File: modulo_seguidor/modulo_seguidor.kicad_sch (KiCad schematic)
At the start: 12 parts, among them J1 Battery, J4 Motor Izquierdo, J5 Motor Derecho, J6 puerto sensores, SW1 SW_Push, U1 LM7806_TO220

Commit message: feat: Asigno las huellas a los componentes
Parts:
- C1: value C -> 1u; footprint (none) -> Capacitor_THT:C_Disc_D7.5mm_W5.0mm_P10.00mm
- C2: footprint (none) -> Capacitor_THT:C_Disc_D7.5mm_W5.0mm_P10.00mm
- D1: footprint (none) -> LED_THT:LED_D3.0mm
- J1: footprint (none) -> Connector_Molex:Molex_KK-254_AE-6410-02A_1x02_P2.54mm_Vertical
- J4, J5: footprint (none) -> Connector:FanPinHeader_1x03_P2.54mm_Vertical
- J6: footprint (none) -> Connector_Harwin:Harwin_M20-89008xx_1x08_P2.54mm_Horizontal
- R1, R2: footprint (none) -> Resistor_THT:R_Axial_DIN0204_L3.6mm_D1.6mm_P5.08mm_Horizontal
- SW1: footprint (none) -> Button_Switch_THT:SW_PUSH_6mm
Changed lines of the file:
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@@
 			)
 		)
-		(property "Footprint" ""
+		(property "Footprint" "Capacitor_THT:C_Disc_D7.5mm_W5.0mm_P10.00mm"
 			(at 77.1652 111.76 0)
 			(effects
@@
 			)
 		)
-		(property "Footprint" ""
+		(property "Footprint" "Button_Switch_THT:SW_PUSH_6mm"
 			(at 113.03 113.03 0)
 			(effects
@@
 			)
 		)
-		(property "Footprint" ""
+		(property "Footprint" "LED_THT:LED_D3.0mm"
 			(at 133.35 62.23 0)
 			(effects
@@
 			)
 		)
-		(property "Footprint" ""
+		(property "Footprint" "Connector:FanPinHeader_1x03_P2.54mm_Vertical"
 			(at 196.85 130.81 0)
 			(effects
@@
 			)
 		)
-		(property "Footprint" ""
+		(property "Footprint" "Connector:FanPinHeader_1x03_P2.54mm_Vertical"
 			(at 171.45 130.81 0)
 			(effects
@@
 			)
 		)
-		(property "Footprint" ""
+		(property "Footprint" "Connector_Harwin:Harwin_M20-89008xx_1x08_P2.54mm_Horizontal"
 			(at 237.49 91.44 0)
 			(effects
@@
 			)
 		)
-		(property "Footprint" ""
+		(property "Footprint" "Resistor_THT:R_Axial_DIN0204_L3.6mm_D1.6mm_P5.08mm_Horizontal"
 			(at 125.984 67.564 90)
 			(effects
@@
 			)
 		)
-		(property "Footprint" ""
+		(property "Footprint" "Connector_Molex:Molex_KK-254_AE-6410-02A_1x02_P2.54mm_Vertical"
 			(at 53.34 69.85 0)
 			(effects
@@
 			)
 		)
-		(property "Footprint" ""
+		(property "Footprint" "Resistor_THT:R_Axial_DIN0204_L3.6mm_D1.6mm_P5.08mm_Horizontal"
 			(at 107.696 123.444 90)
 			(effects
@@
 			)
 		)
-		(property "Value" "C"
+		(property "Value" "1u"
 			(at 76.2 69.8499 0)
 			(effects
@@
 			)
 		)
-		(property "Footprint" ""
+		(property "Footprint" "Capacitor_THT:C_Disc_D7.5mm_W5.0mm_P10.00mm"
 			(at 73.3552 72.39 0)
 			(effects

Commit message: refactor: Actualizo huellas del esquemático
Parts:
- C1, C2: footprint Capacitor_THT:C_Disc_D7.5mm_W5.0mm_P10.00mm -> Capacitor_THT:C_Disc_D7.0mm_W2.5mm_P5.00mm
- D1: footprint LED_THT:LED_D3.0mm -> LED_THT:LED_D5.0mm
- J4, J5: footprint Connector:FanPinHeader_1x03_P2.54mm_Vertical -> Connector_PinHeader_2.54mm:PinHeader_1x03_P2.54mm_Vertical
- J6: footprint Connector_Harwin:Harwin_M20-89008xx_1x08_P2.54mm_Horizontal -> Connector_PinHeader_2.54mm:PinHeader_1x08_P2.54mm_Horizontal
- R1, R2: footprint Resistor_THT:R_Axial_DIN0204_L3.6mm_D1.6mm_P5.08mm_Horizontal -> Resistor_THT:R_Axial_DIN0411_L9.9mm_D3.6mm_P12.70mm_Horizontal
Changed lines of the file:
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@@
 			)
 		)
-		(property "Footprint" "Capacitor_THT:C_Disc_D7.5mm_W5.0mm_P10.00mm"
+		(property "Footprint" "Capacitor_THT:C_Disc_D7.0mm_W2.5mm_P5.00mm"
 			(at 77.1652 111.76 0)
 			(effects
@@
 			)
 		)
-		(property "Footprint" "LED_THT:LED_D3.0mm"
+		(property "Footprint" "LED_THT:LED_D5.0mm"
 			(at 133.35 62.23 0)
 			(effects
@@
 			)
 		)
-		(property "Footprint" "Connector:FanPinHeader_1x03_P2.54mm_Vertical"
+		(property "Footprint" "Connector_PinHeader_2.54mm:PinHeader_1x03_P2.54mm_Vertical"
 			(at 196.85 130.81 0)
 			(effects
@@
 			)
 		)
-		(property "Footprint" "Connector:FanPinHeader_1x03_P2.54mm_Vertical"
+		(property "Footprint" "Connector_PinHeader_2.54mm:PinHeader_1x03_P2.54mm_Vertical"
 			(at 171.45 130.81 0)
 			(effects
@@
 			)
 		)
-		(property "Footprint" "Connector_Harwin:Harwin_M20-89008xx_1x08_P2.54mm_Horizontal"
+		(property "Footprint" "Connector_PinHeader_2.54mm:PinHeader_1x08_P2.54mm_Horizontal"
 			(at 237.49 91.44 0)
 			(effects
@@
 			)
 		)
-		(property "Footprint" "Resistor_THT:R_Axial_DIN0204_L3.6mm_D1.6mm_P5.08mm_Horizontal"
+		(property "Footprint" "Resistor_THT:R_Axial_DIN0411_L9.9mm_D3.6mm_P12.70mm_Horizontal"
 			(at 125.984 67.564 90)
 			(effects
@@
 			)
 		)
-		(property "Footprint" "Resistor_THT:R_Axial_DIN0204_L3.6mm_D1.6mm_P5.08mm_Horizontal"
+		(property "Footprint" "Resistor_THT:R_Axial_DIN0411_L9.9mm_D3.6mm_P12.70mm_Horizontal"
 			(at 107.696 123.444 90)
 			(effects
@@
 			)
 		)
-		(property "Footprint" "Capacitor_THT:C_Disc_D7.5mm_W5.0mm_P10.00mm"
+		(property "Footprint" "Capacitor_THT:C_Disc_D7.0mm_W2.5mm_P5.00mm"
 			(at 73.3552 72.39 0)
 			(effects

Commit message: refactor: Cambio las conexiones en los pines del modulo seguidor para compactar la pcb
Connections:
- net Boton_encendido: now also A2.D10; no longer A2.D2 (D2_INT0)
- net PWM_DER: now also A2.D8; no longer A2.D9
- net PWM_IZQ: now also A2.D9; no longer A2.D10
- net Sensor1: now also A2.D7; no longer A2.D8
- net Sensor2: now also A2.D6; no longer A2.D7
- net Sensor3: now also A2.D5; no longer A2.D6
- net Sensor4: now also A2.D4; no longer A2.D5
- net Sensor5: now also A2.D3 (D3_INT1); no longer A2.D4
- net Sensor6: now also A2.D2 (D2_INT0); no longer A2.D3 (D3_INT1)
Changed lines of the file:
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@@
 	)
 	(label "Sensor1"
-		(at 190.5 67.31 0)
+		(at 190.5 64.77 0)
 		(fields_autoplaced yes)
 		(effects
@@
 	)
 	(label "PWM_IZQ"
-		(at 190.5 72.39 0)
+		(at 190.5 69.85 0)
 		(fields_autoplaced yes)
 		(effects
@@
 	)
 	(label "Sensor3"
-		(at 190.5 62.23 0)
+		(at 190.5 59.69 0)
 		(fields_autoplaced yes)
 		(effects
@@
 	)
 	(label "Boton_encendido"
-		(at 190.5 52.07 0)
+		(at 190.5 72.39 0)
 		(fields_autoplaced yes)
 		(effects
@@
 	)
 	(label "Sensor2"
-		(at 190.5 64.77 0)
+		(at 190.5 62.23 0)
 		(fields_autoplaced yes)
 		(effects
@@
 	)
 	(label "Sensor4"
-		(at 190.5 59.69 0)
+		(at 190.5 57.15 0)
 		(fields_autoplaced yes)
 		(effects
@@
 	)
 	(label "PWM_DER"
-		(at 190.5 69.85 0)
+		(at 190.5 67.31 0)
 		(fields_autoplaced yes)
 		(effects
@@
 	)
 	(label "Sensor5"
-		(at 190.5 57.15 0)
+		(at 190.5 54.61 0)
 		(fields_autoplaced yes)
 		(effects
@@
 	)
 	(label "Sensor6"
-		(at 190.5 54.61 0)
+		(at 190.5 52.07 0)
 		(fields_autoplaced yes)
 		(effects

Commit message: refactor(modulo_seguidor): Intercambio dos pines para hacer los cables más cortos
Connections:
- net Boton_encendido: now also A2.D8; no longer A2.D10
- net PWM_DER: now also A2.D9; no longer A2.D8
- net PWM_IZQ: now also A2.D10; no longer A2.D9
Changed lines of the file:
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@@
 	)
 	(label "PWM_IZQ"
-		(at 190.5 69.85 0)
+		(at 190.5 72.39 0)
 		(fields_autoplaced yes)
 		(effects
@@
 	)
 	(label "Boton_encendido"
-		(at 190.5 72.39 0)
+		(at 190.5 67.31 0)
 		(fields_autoplaced yes)
 		(effects
@@
 	)
 	(label "PWM_DER"
-		(at 190.5 67.31 0)
+		(at 190.5 69.85 0)
 		(fields_autoplaced yes)
 		(effects

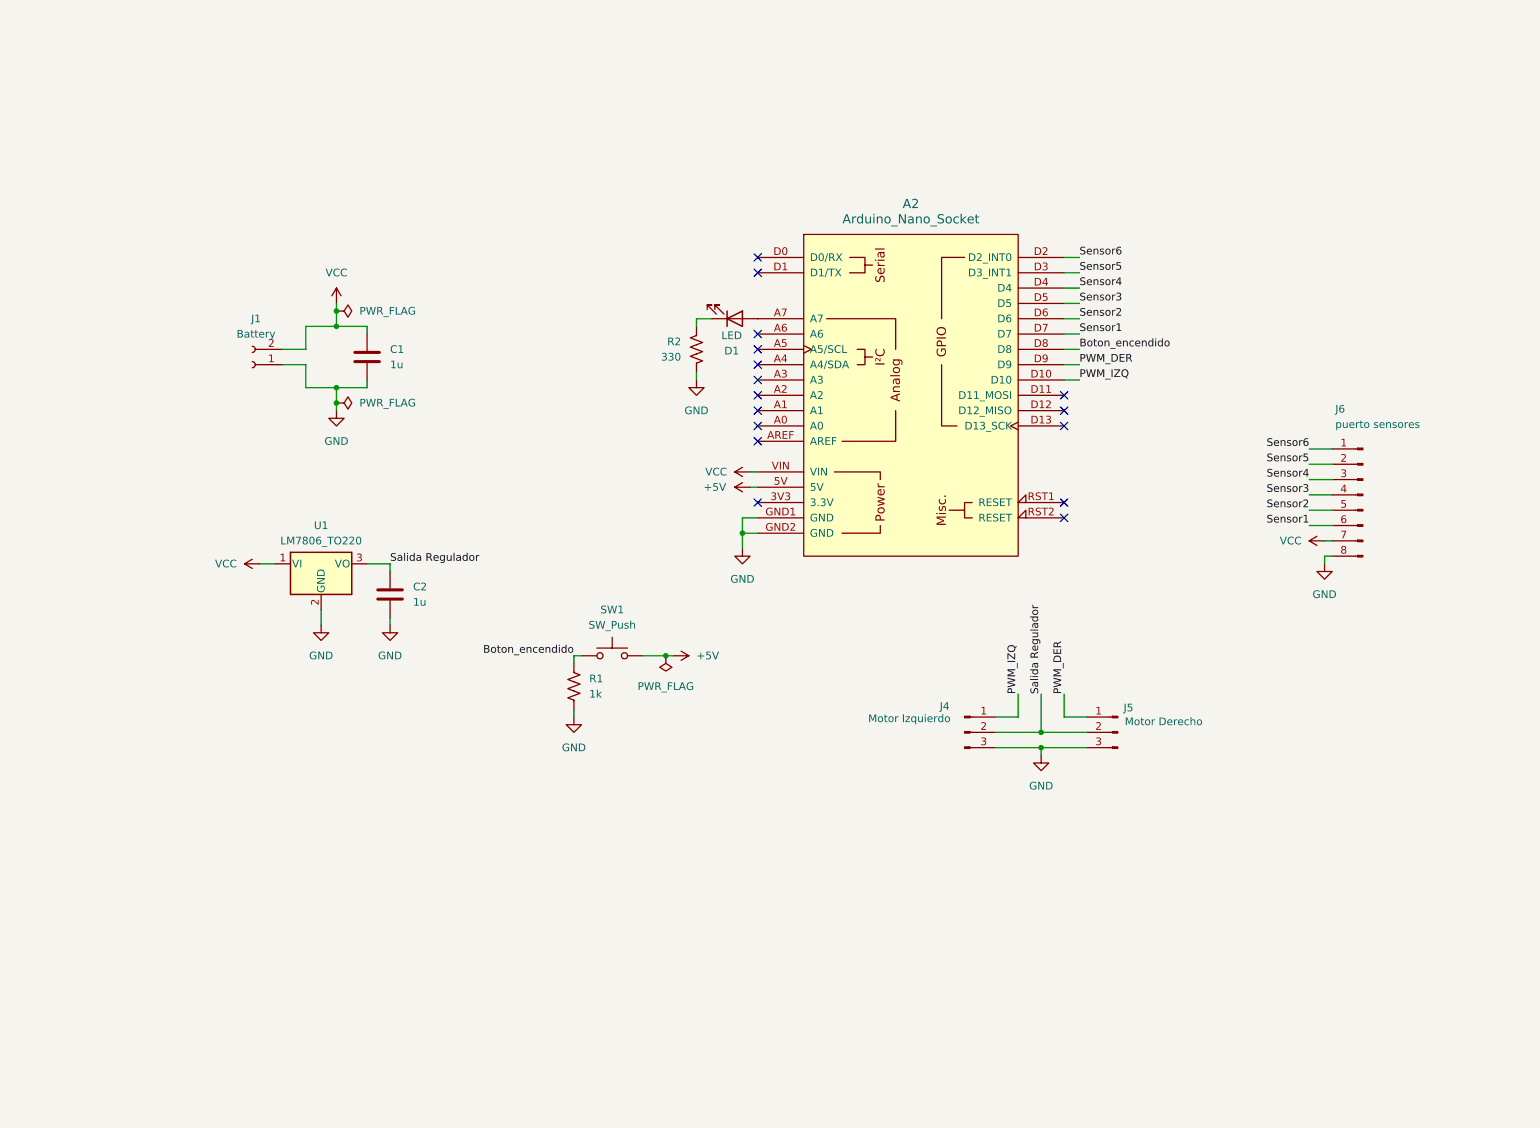
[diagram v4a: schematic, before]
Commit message: feat(seguidor): Agrego puente H y motores al esquemático
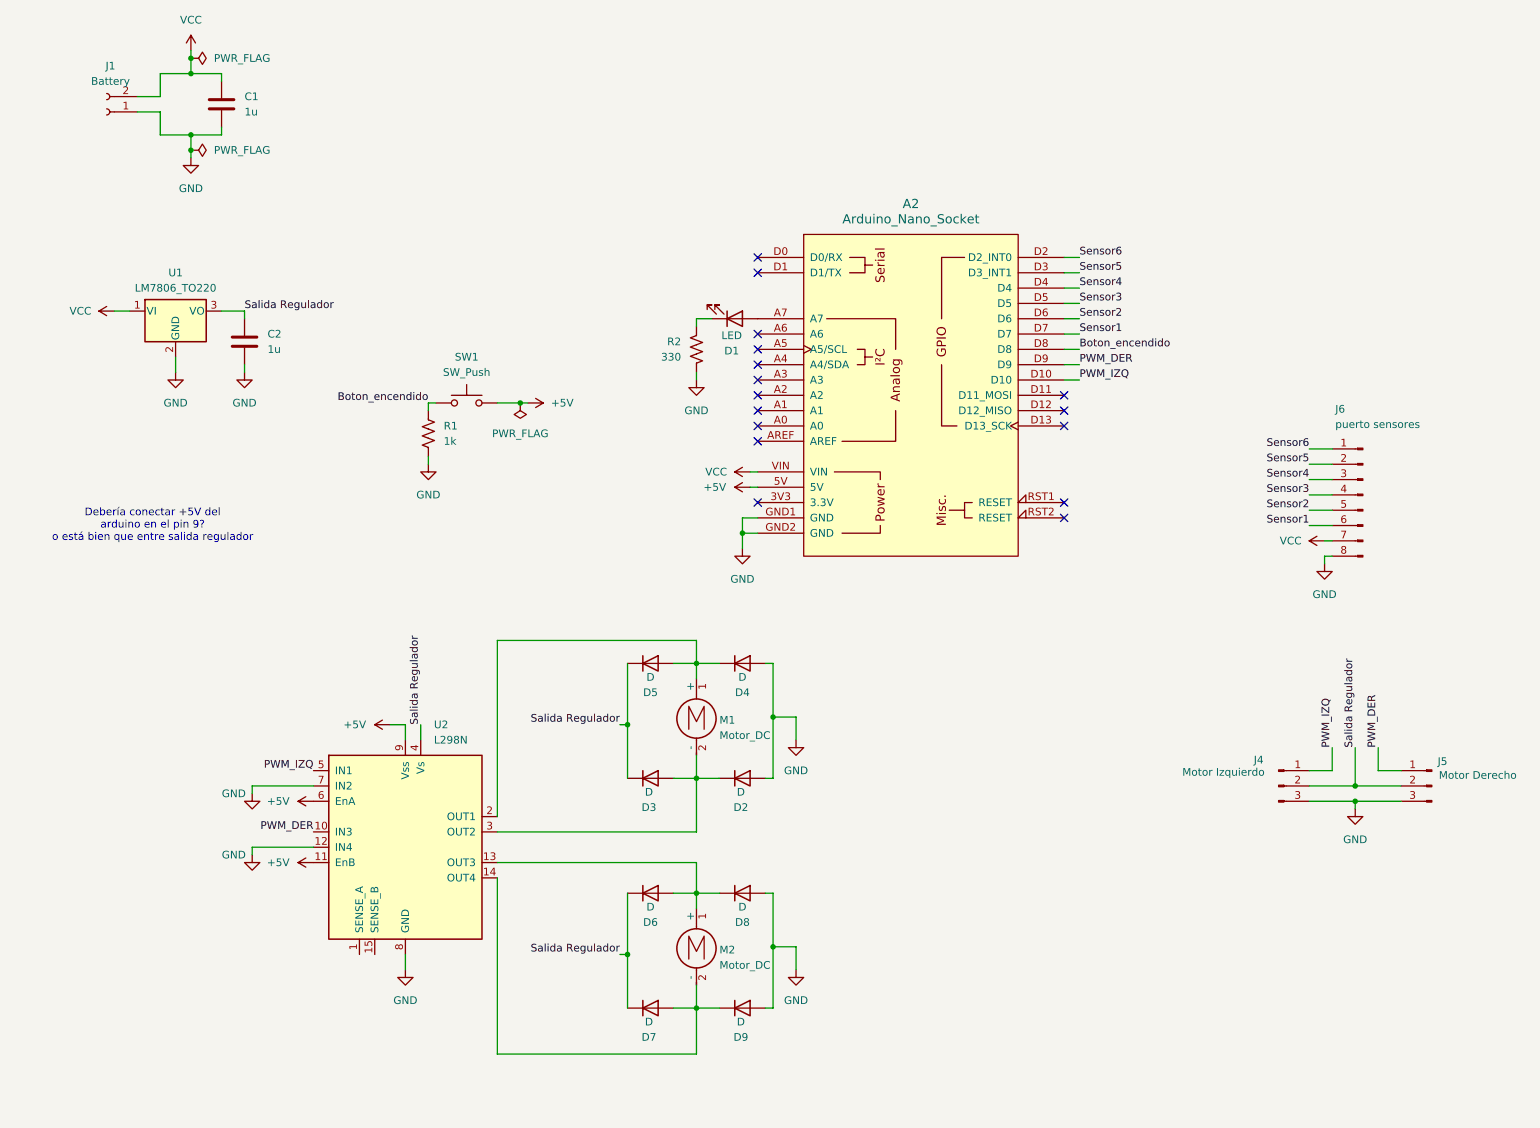
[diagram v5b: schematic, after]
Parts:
- added D2, D3, D4, D5, D6, D7, D8, D9: D, symbol Device:D
- added M1, M2: Motor_DC, symbol Motor:Motor_DC
- added U2: L298N, Package_TO_SOT_THT:TO-220-15_P2.54x2.54mm_StaggerOdd_Lead4.58mm_Vertical, symbol Driver_Motor:L298N
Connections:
- net +5V: now also U2.11 (EnB), U2.6 (EnA), U2.9 (Vss)
- net GND: now also D2.2 (A), D4.2 (A), D8.2 (A), D9.2 (A), U2.12 (IN4), U2.7 (IN2), U2.8 (GND)
- net PWM_DER: now also U2.10 (IN3)
- net PWM_IZQ: now also U2.5 (IN1)
- net Salida Regulador: now also D3.1 (K), D5.1 (K), D6.1 (K), D7.1 (K), U2.4 (Vs)
- new net: D4.1 (K), D5.2 (A), M1.1 (+), U2.2 (OUT1)
- new net: D6.2 (A), D8.1 (K), M2.1 (+), U2.13 (OUT3)
- new net: D7.2 (A), D9.1 (K), M2.2 (-), U2.14 (OUT4)
- new net: D2.1 (K), D3.2 (A), M1.2 (-), U2.3 (OUT2)
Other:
- note added: "Debería conectar +5V del arduino en el pin 9? o está bien que entre salida regulador"
- moved on the sheet: C1, C2, J1, J4, J5, R1, SW1, U1

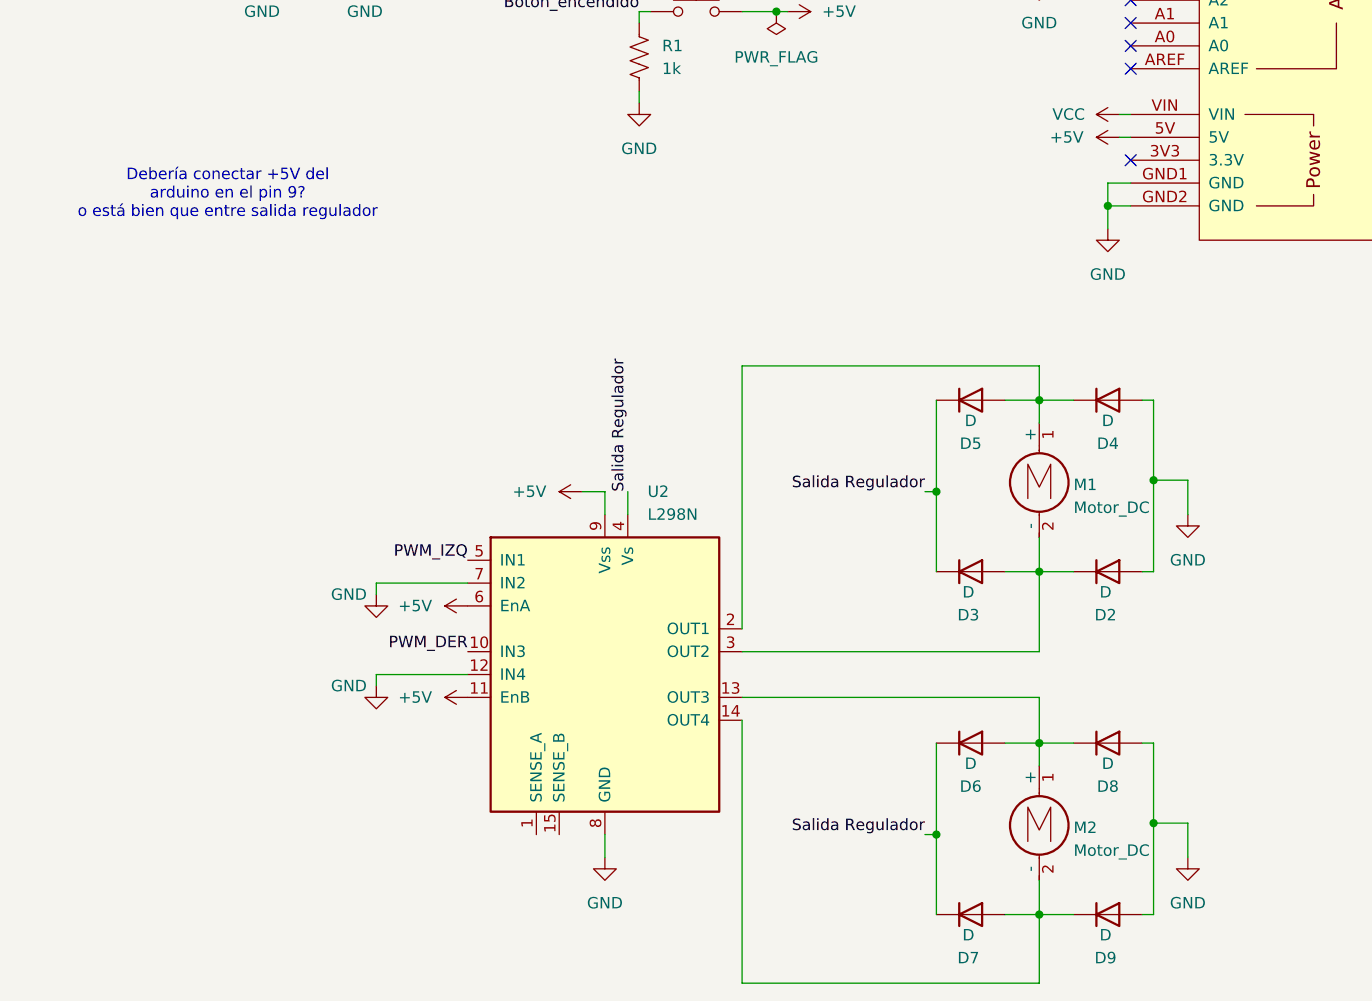
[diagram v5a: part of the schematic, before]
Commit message: feat(puente-h): Agrego esquemático del puente H
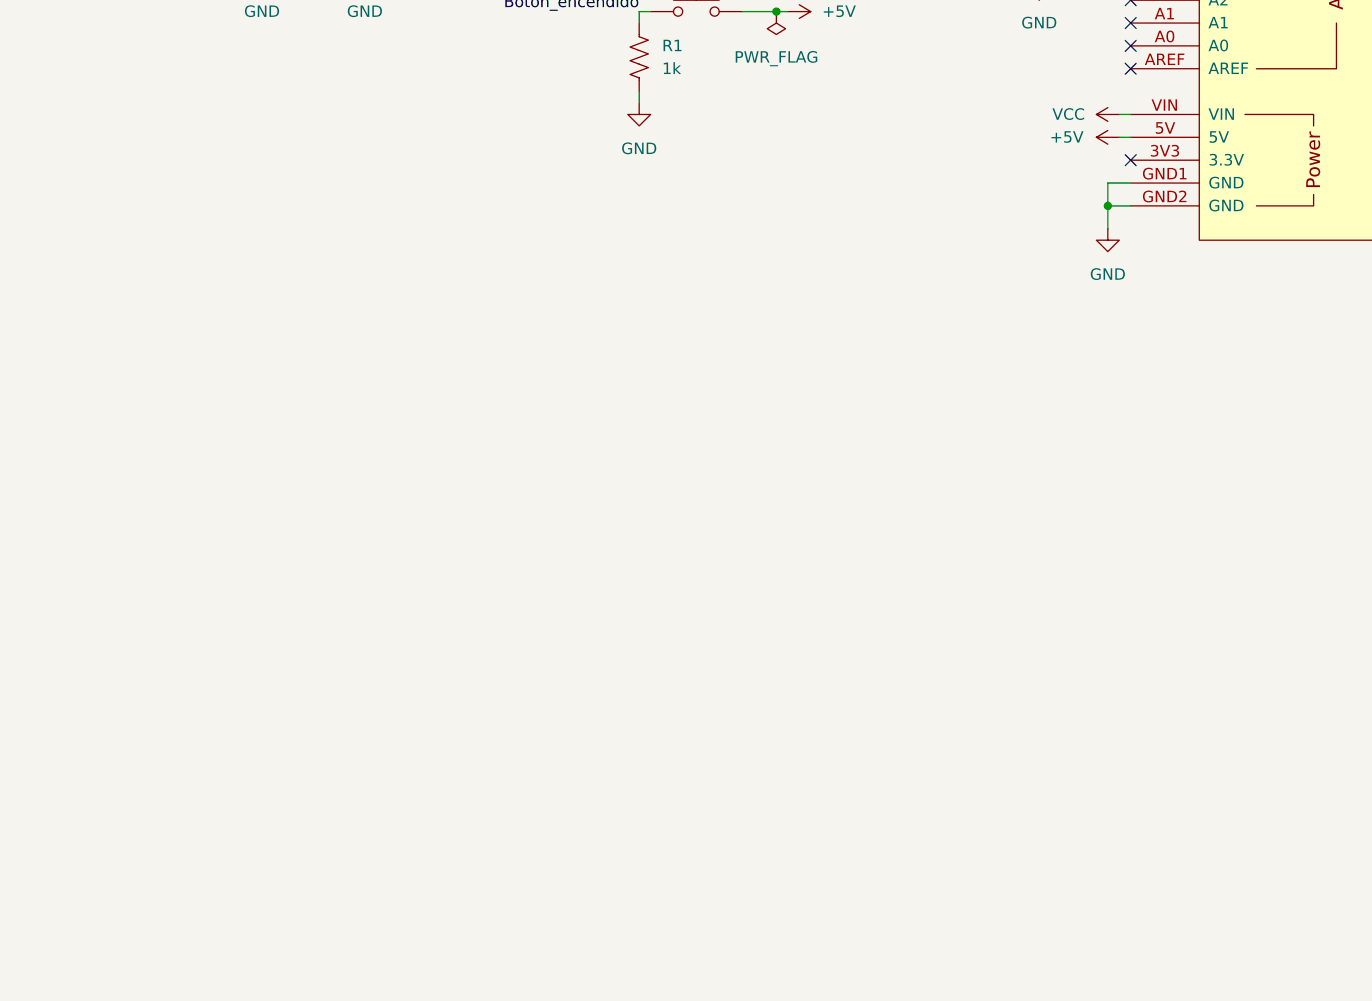
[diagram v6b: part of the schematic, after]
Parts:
- removed D2, D3, D4, D5, D6, D7, D8, D9: D, symbol Device:D
- removed M1, M2: Motor_DC, symbol Motor:Motor_DC
- removed U2: L298N, Package_TO_SOT_THT:TO-220-15_P2.54x2.54mm_StaggerOdd_Lead4.58mm_Vertical, symbol Driver_Motor:L298N
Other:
- note removed: "Debería conectar +5V del arduino en el pin 9? o está bien que entre salida regulador"
